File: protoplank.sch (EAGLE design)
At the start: 109 parts, among them IC1 74AHC1G86DBV

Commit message: Updated protoplank to use square pads for ease of SMT soldering.
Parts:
- U$100, U$101, U$102, U$103, U$23, U$24, U$25, U$26, U$34, U$35, U$36, U$37, U$38, U$39, U$40, U$41, U$42, U$43, U$44, U$45, U$46, U$47, U$48, U$49, U$50, U$51, U$52, U$53, U$54, U$55, U$56, U$57, U$58, U$59, U$60, U$61, U$62, U$63, U$64, U$65, U$66, U$67, U$68, U$69, U$70, U$71, U$72, U$73, U$74, U$75, U$76, U$77, U$79, U$81, U$82, U$83, U$84, U$85, U$86, U$87, U$88, U$89, U$90, U$91, U$92, U$93, U$94, U$95, U$96, U$97, U$98, U$99: value PROTOPAD-4 -> PROTOPAD-4SQUARE; device nickparts:PROTOPAD-4 -> nickparts:PROTOPAD-4SQUARE
- U$104, U$105, U$106, U$107, U$27, U$28: value PROTOPAD-2 -> PROTOPAD-2SQUARE; device nickparts:PROTOPAD-2 -> nickparts:PROTOPAD-2SQUARE
- U$29, U$30, U$31, U$32: value PROTOPAD-4 -> PROTOPAD-4ROUND; device nickparts:PROTOPAD-4 -> nickparts:PROTOPAD-4ROUND
- U$33: value PROTOPAD-2 -> PROTOPAD-2ROUND; device nickparts:PROTOPAD-2 -> nickparts:PROTOPAD-2ROUND

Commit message: Added decoupling capacitors to the protoboard.
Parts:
- added C1, C2: (no value), SparkFun-Passives:CAPPTH
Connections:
- net +3V3: now also C1.1
- net +5V: now also C2.1
- net GND: now also C1.2, C2.2
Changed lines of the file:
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@@
 <part name="U$106" library="nickparts" deviceset="PROTOPAD-2" device="SQUARE"/>
 <part name="U$107" library="nickparts" deviceset="PROTOPAD-2" device="SQUARE"/>
+<part name="+3V6" library="supply1" deviceset="+3V3" device=""/>
+<part name="P+4" library="supply1" deviceset="+5V" device=""/>
+<part name="GND7" library="supply1" deviceset="GND" device=""/>
+<part name="C1" library="SparkFun-Passives" deviceset="CAP" device="PTH"/>
+<part name="C2" library="SparkFun-Passives" deviceset="CAP" device="PTH"/>
 </parts>
 <sheets>
@@
 <instance part="U$106" gate="G$1" x="119.38" y="154.94"/>
 <instance part="U$107" gate="G$1" x="119.38" y="73.66"/>
+<instance part="+3V6" gate="G$1" x="279.4" y="78.74"/>
+<instance part="P+4" gate="1" x="287.02" y="78.74"/>
+<instance part="GND7" gate="1" x="279.4" y="58.42"/>
+<instance part="C1" gate="G$1" x="279.4" y="66.04"/>
+<instance part="C2" gate="G$1" x="287.02" y="66.04"/>
 </instances>
 <busses>
@@
 <junction x="251.46" y="121.92"/>
 </segment>
+<segment>
+<pinref part="+3V6" gate="G$1" pin="+3V3"/>
+<pinref part="C1" gate="G$1" pin="1"/>
+<wire x1="279.4" y1="76.2" x2="279.4" y2="71.12" width="0.1524" layer="91"/>
+</segment>
 </net>
 <net name="GND" class="0">
@@
 <junction x="256.54" y="91.44"/>
 </segment>
+<segment>
+<pinref part="GND7" gate="1" pin="GND"/>
+<pinref part="C1" gate="G$1" pin="2"/>
+<wire x1="279.4" y1="60.96" x2="279.4" y2="63.5" width="0.1524" layer="91"/>
+<pinref part="C2" gate="G$1" pin="2"/>
+<wire x1="287.02" y1="63.5" x2="279.4" y2="63.5" width="0.1524" layer="91"/>
+<junction x="279.4" y="63.5"/>
+</segment>
 </net>
 <net name="A0" class="0">
@@
 <junction x="256.54" y="121.92"/>
 </segment>
-</net>
+<segment>
+<pinref part="P+4" gate="1" pin="+5V"/>
+<pinref part="C2" gate="G$1" pin="1"/>
+<wire x1="287.02" y1="76.2" x2="287.02" y2="71.12" width="0.1524" layer="91"/>
+</segment>
+</net>

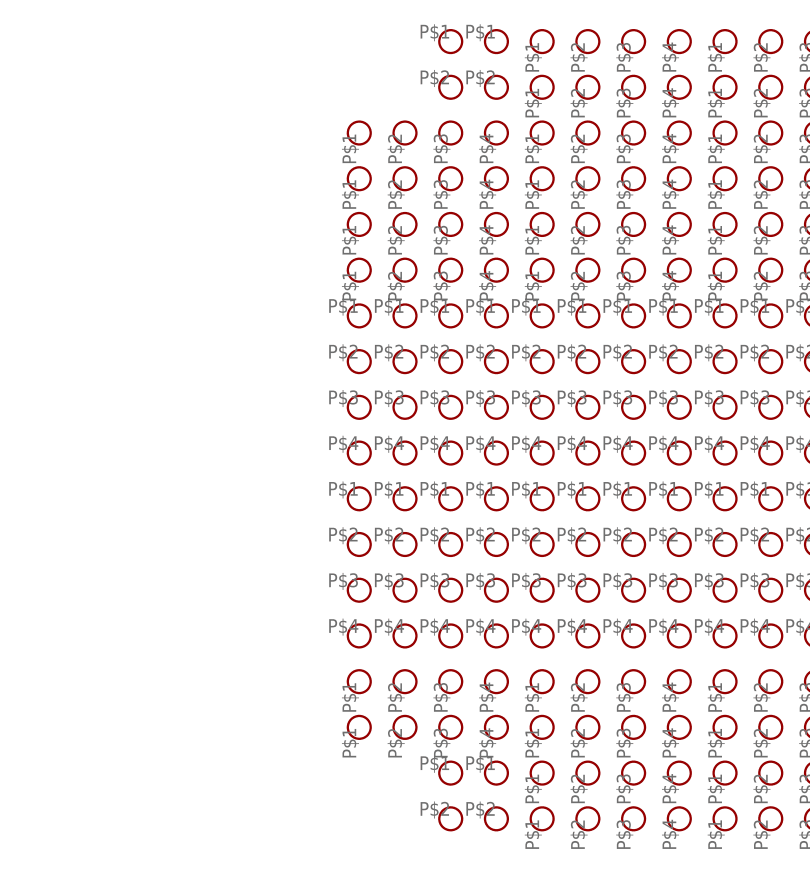
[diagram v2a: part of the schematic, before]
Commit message: Added tripads for edge connectors on protoshield.
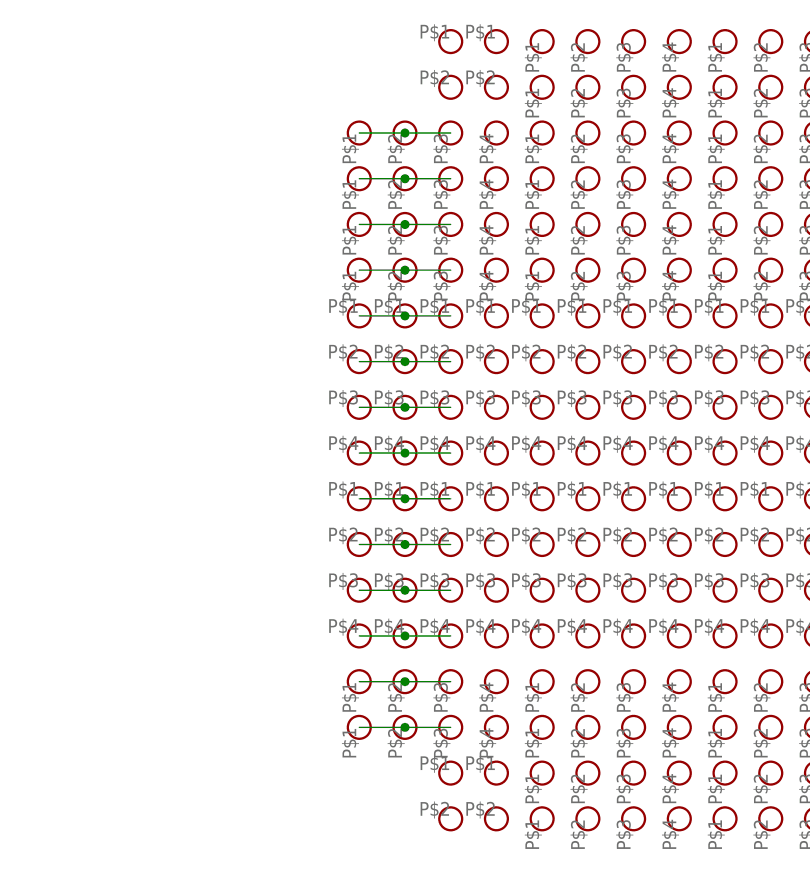
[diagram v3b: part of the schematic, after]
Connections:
- new net N$54: U$89.P$1, U$89.P$2, U$89.P$3
- new net N$55: U$88.P$1, U$88.P$2, U$88.P$3
- new net N$58: U$81.P$1, U$81.P$2, U$81.P$3
- new net N$61: U$76.P$1, U$76.P$2, U$76.P$3
- new net N$62: U$65.P$1, U$66.P$1, U$69.P$1
- new net N$63: U$65.P$2, U$66.P$2, U$69.P$2
- new net N$64: U$65.P$3, U$66.P$3, U$69.P$3
- new net N$65: U$65.P$4, U$66.P$4, U$69.P$4
- new net N$66: U$64.P$1, U$67.P$1, U$68.P$1
- new net N$67: U$64.P$2, U$67.P$2, U$68.P$2
- new net N$68: U$64.P$3, U$67.P$3, U$68.P$3
- new net N$69: U$64.P$4, U$67.P$4, U$68.P$4
- new net N$70: U$96.P$1, U$96.P$2, U$96.P$3
- new net N$71: U$99.P$1, U$99.P$2, U$99.P$3
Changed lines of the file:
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@@
+</segment>
+</net>
+<net name="N$54" class="0">
+<segment>
+<pinref part="U$89" gate="G$1" pin="P$1"/>
+<pinref part="U$89" gate="G$1" pin="P$2"/>
+<wire x1="109.22" y1="147.32" x2="114.3" y2="147.32" width="0.1524" layer="91"/>
+<pinref part="U$89" gate="G$1" pin="P$3"/>
+<wire x1="114.3" y1="147.32" x2="119.38" y2="147.32" width="0.1524" layer="91"/>
+<junction x="114.3" y="147.32"/>
+</segment>
+</net>
+<net name="N$55" class="0">
+<segment>
+<pinref part="U$88" gate="G$1" pin="P$3"/>
+<pinref part="U$88" gate="G$1" pin="P$2"/>
+<wire x1="119.38" y1="142.24" x2="114.3" y2="142.24" width="0.1524" layer="91"/>
+<pinref part="U$88" gate="G$1" pin="P$1"/>
+<wire x1="114.3" y1="142.24" x2="109.22" y2="142.24" width="0.1524" layer="91"/>
+<junction x="114.3" y="142.24"/>
+</segment>
+</net>
+<net name="N$58" class="0">
+<segment>
+<pinref part="U$81" gate="G$1" pin="P$1"/>
+<pinref part="U$81" gate="G$1" pin="P$2"/>
+<wire x1="109.22" y1="137.16" x2="114.3" y2="137.16" width="0.1524" layer="91"/>
+<pinref part="U$81" gate="G$1" pin="P$3"/>
+<wire x1="114.3" y1="137.16" x2="119.38" y2="137.16" width="0.1524" layer="91"/>
+<junction x="114.3" y="137.16"/>
+</segment>
+</net>
+<net name="N$61" class="0">
+<segment>
+<pinref part="U$76" gate="G$1" pin="P$3"/>
+<pinref part="U$76" gate="G$1" pin="P$2"/>
+<wire x1="119.38" y1="132.08" x2="114.3" y2="132.08" width="0.1524" layer="91"/>
+<pinref part="U$76" gate="G$1" pin="P$1"/>
+<wire x1="114.3" y1="132.08" x2="109.22" y2="132.08" width="0.1524" layer="91"/>
+<junction x="114.3" y="132.08"/>
+</segment>
+</net>
+<net name="N$62" class="0">
+<segment>
+<pinref part="U$69" gate="G$1" pin="P$1"/>
+<pinref part="U$66" gate="G$1" pin="P$1"/>
+<wire x1="109.22" y1="127" x2="114.3" y2="127" width="0.1524" layer="91"/>
+<pinref part="U$65" gate="G$1" pin="P$1"/>
+<wire x1="114.3" y1="127" x2="119.38" y2="127" width="0.1524" layer="91"/>
+<junction x="114.3" y="127"/>
+</segment>
+</net>
+<net name="N$63" class="0">
+<segment>
+<pinref part="U$65" gate="G$1" pin="P$2"/>
+<pinref part="U$66" gate="G$1" pin="P$2"/>
+<wire x1="119.38" y1="121.92" x2="114.3" y2="121.92" width="0.1524" layer="91"/>
+<pinref part="U$69" gate="G$1" pin="P$2"/>
+<wire x1="114.3" y1="121.92" x2="109.22" y2="121.92" width="0.1524" layer="91"/>
+<junction x="114.3" y="121.92"/>
+</segment>
+</net>
+<net name="N$64" class="0">
+<segment>
+<pinref part="U$69" gate="G$1" pin="P$3"/>
+<pinref part="U$66" gate="G$1" pin="P$3"/>
+<wire x1="109.22" y1="116.84" x2="114.3" y2="116.84" width="0.1524" layer="91"/>
+<pinref part="U$65" gate="G$1" pin="P$3"/>
+<wire x1="114.3" y1="116.84" x2="119.38" y2="116.84" width="0.1524" layer="91"/>
+<junction x="114.3" y="116.84"/>
+</segment>
+</net>
+<net name="N$65" class="0">
+<segment>
+<pinref part="U$69" gate="G$1" pin="P$4"/>
+<pinref part="U$66" gate="G$1" pin="P$4"/>
+<wire x1="109.22" y1="111.76" x2="114.3" y2="111.76" width="0.1524" layer="91"/>
+<pinref part="U$65" gate="G$1" pin="P$4"/>
+<wire x1="114.3" y1="111.76" x2="119.38" y2="111.76" width="0.1524" layer="91"/>
+<junction x="114.3" y="111.76"/>
+</segment>
+</net>
+<net name="N$66" class="0">
+<segment>
+<pinref part="U$64" gate="G$1" pin="P$1"/>
+<pinref part="U$67" gate="G$1" pin="P$1"/>
+<wire x1="119.38" y1="106.68" x2="114.3" y2="106.68" width="0.1524" layer="91"/>
+<pinref part="U$68" gate="G$1" pin="P$1"/>
+<wire x1="114.3" y1="106.68" x2="109.22" y2="106.68" width="0.1524" layer="91"/>
+<junction x="114.3" y="106.68"/>
+</segment>
+</net>
+<net name="N$67" class="0">
+<segment>
+<pinref part="U$68" gate="G$1" pin="P$2"/>
+<pinref part="U$67" gate="G$1" pin="P$2"/>
+<wire x1="109.22" y1="101.6" x2="114.3" y2="101.6" width="0.1524" layer="91"/>
+<pinref part="U$64" gate="G$1" pin="P$2"/>
+<wire x1="114.3" y1="101.6" x2="119.38" y2="101.6" width="0.1524" layer="91"/>
+<junction x="114.3" y="101.6"/>
+</segment>
+</net>
+<net name="N$68" class="0">
+<segment>
+<pinref part="U$64" gate="G$1" pin="P$3"/>
+<pinref part="U$67" gate="G$1" pin="P$3"/>
+<wire x1="119.38" y1="96.52" x2="114.3" y2="96.52" width="0.1524" layer="91"/>
+<pinref part="U$68" gate="G$1" pin="P$3"/>
+<wire x1="114.3" y1="96.52" x2="109.22" y2="96.52" width="0.1524" layer="91"/>
+<junction x="114.3" y="96.52"/>
+</segment>
+</net>
+<net name="N$69" class="0">
+<segment>
+<pinref part="U$68" gate="G$1" pin="P$4"/>
+<pinref part="U$67" gate="G$1" pin="P$4"/>
+<wire x1="109.22" y1="91.44" x2="114.3" y2="91.44" width="0.1524" layer="91"/>
+<pinref part="U$64" gate="G$1" pin="P$4"/>
+<wire x1="114.3" y1="91.44" x2="119.38" y2="91.44" width="0.1524" layer="91"/>
+<junction x="114.3" y="91.44"/>
+</segment>
+</net>
+<net name="N$70" class="0">
+<segment>
+<pinref part="U$96" gate="G$1" pin="P$3"/>
+<pinref part="U$96" gate="G$1" pin="P$2"/>
+<wire x1="119.38" y1="86.36" x2="114.3" y2="86.36" width="0.1524" layer="91"/>
+<pinref part="U$96" gate="G$1" pin="P$1"/>
+<wire x1="114.3" y1="86.36" x2="109.22" y2="86.36" width="0.1524" layer="91"/>
+<junction x="114.3" y="86.36"/>
+</segment>
+</net>
+<net name="N$71" class="0">
+<segment>
+<pinref part="U$99" gate="G$1" pin="P$1"/>
+<pinref part="U$99" gate="G$1" pin="P$2"/>
+<wire x1="109.22" y1="81.28" x2="114.3" y2="81.28" width="0.1524" layer="91"/>
+<pinref part="U$99" gate="G$1" pin="P$3"/>
+<wire x1="114.3" y1="81.28" x2="119.38" y2="81.28" width="0.1524" layer="91"/>
+<junction x="114.3" y="81.28"/>
 </segment>
 </net>
